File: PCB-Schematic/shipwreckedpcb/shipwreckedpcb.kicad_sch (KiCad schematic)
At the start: 180 parts, among them J1 USB4105, J14 Conn_01x01, J15 Conn_01x01, J16 Conn_01x01, J17 Conn_01x01, J18 Conn_01x01, J19 Conn_01x01, J2 Waveshare 1.54" E-Ink, J20 Conn_01x01, J21 Conn_01x01, J22 Conn_01x01, J23 Conn_01x01, J24 Conn_01x01, J25 Conn_01x01, J26 Conn_01x01, J28 Conn_01x01, J29 Conn_01x01, J3 Conn_01x01, J30 Conn_01x01, J31 Conn_01x01, J32 Conn_01x01, J33 Conn_01x01, J34 Conn_01x01, J35 Conn_01x01, J36 Conn_01x01, J37 Conn_01x01, J38 Conn_01x01, J39 Conn_01x01, J4 Conn_01x01, J5 SWD, J6 Conn_01x01, J7 Conn_01x01, Q1 Si1308EDL, SW1 BOOTSEL, SW10 Resistive, SW11 Clicky - THT, SW12 Clicky - SMD, SW13 Clicky - THT, SW14 Clicky - SMD, SW15 Clicky - THT, SW16 Clicky - SMD, SW17 Clicky - THT, SW18 Clicky - SMD, SW19 PWR Switch, SW2 RESET, SW3 Resistive, SW4 Resistive, SW5 Resistive, SW6 Resistive, SW7 Resistive, SW8 Resistive, SW9 Resistive, U1 RP2040, U2 W25Q128JVS, U3 Si4463, U4 TPS61200DRC, U5 AS179-92LF, U7 PCA9555PW, U8 ST25DV04K-IE6S3, Y1 ABM8-272-T3, Y2 X322530MOB4SI

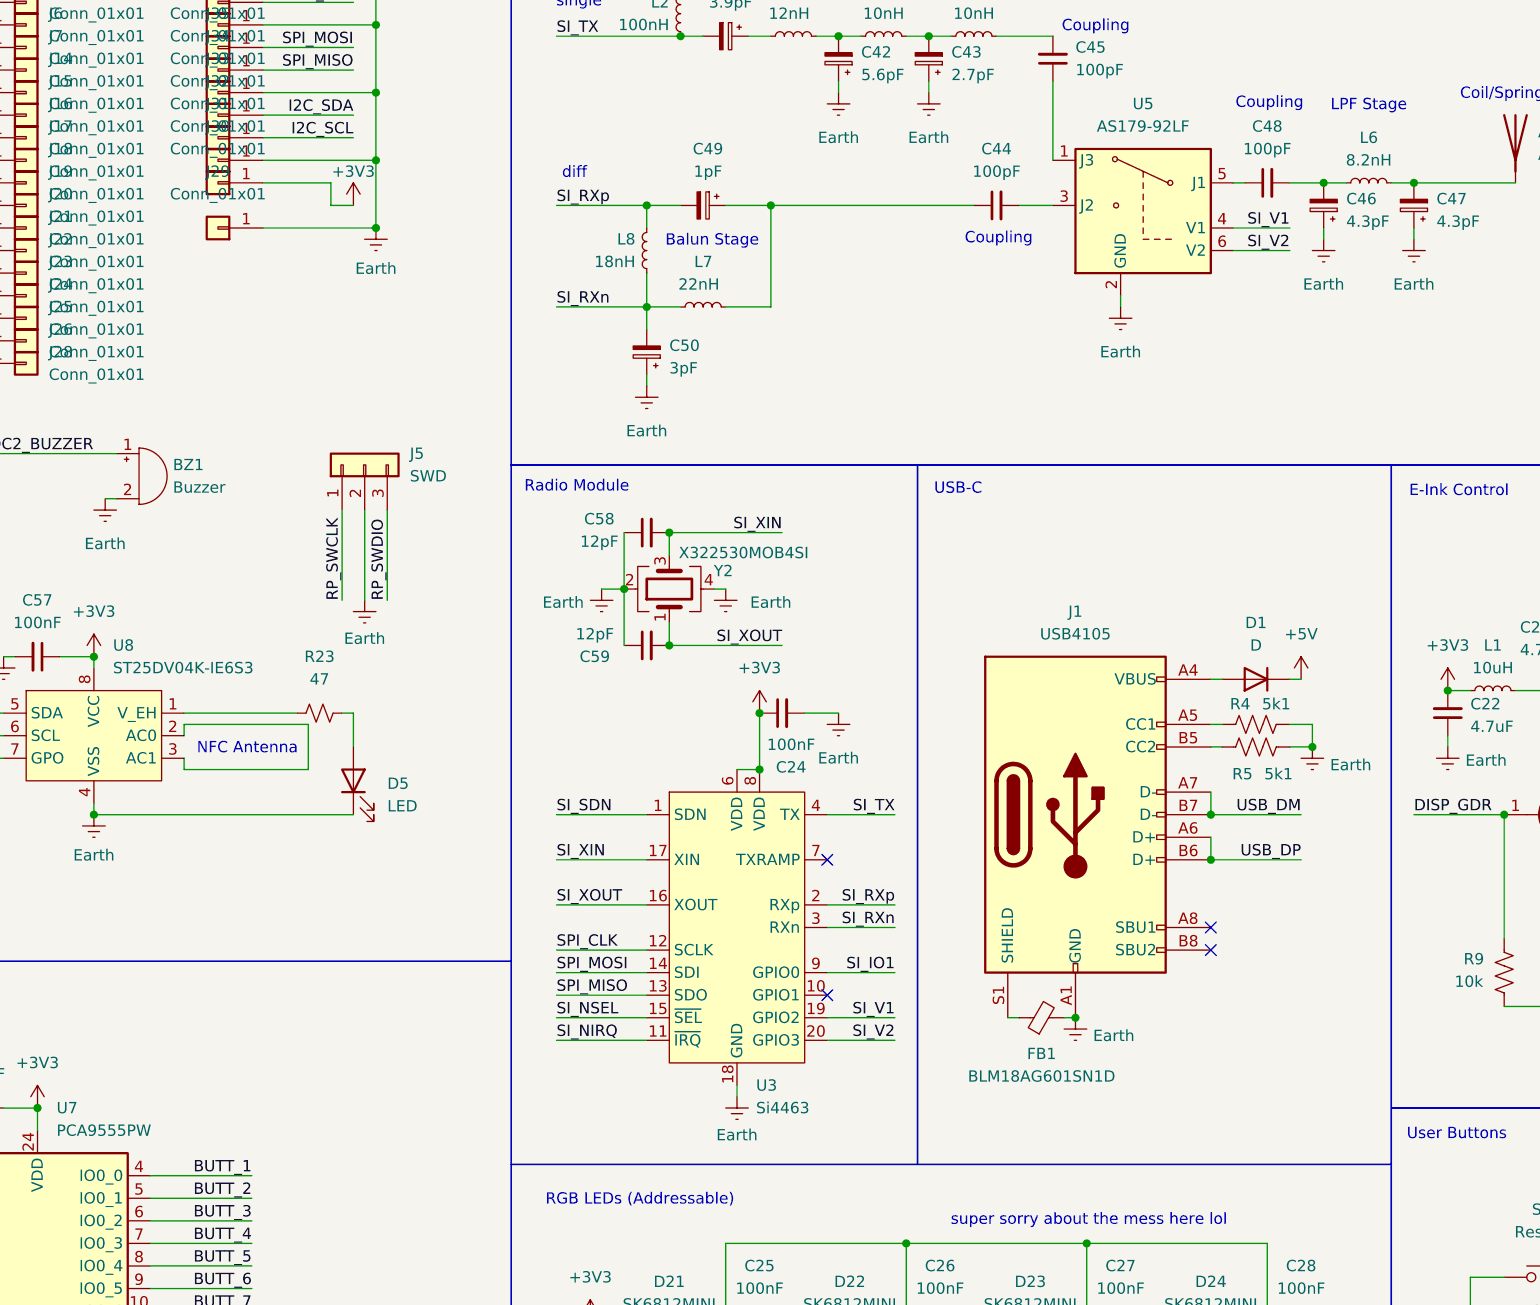
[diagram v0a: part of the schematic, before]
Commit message: boost conv, leds, caps, added ldo for usb
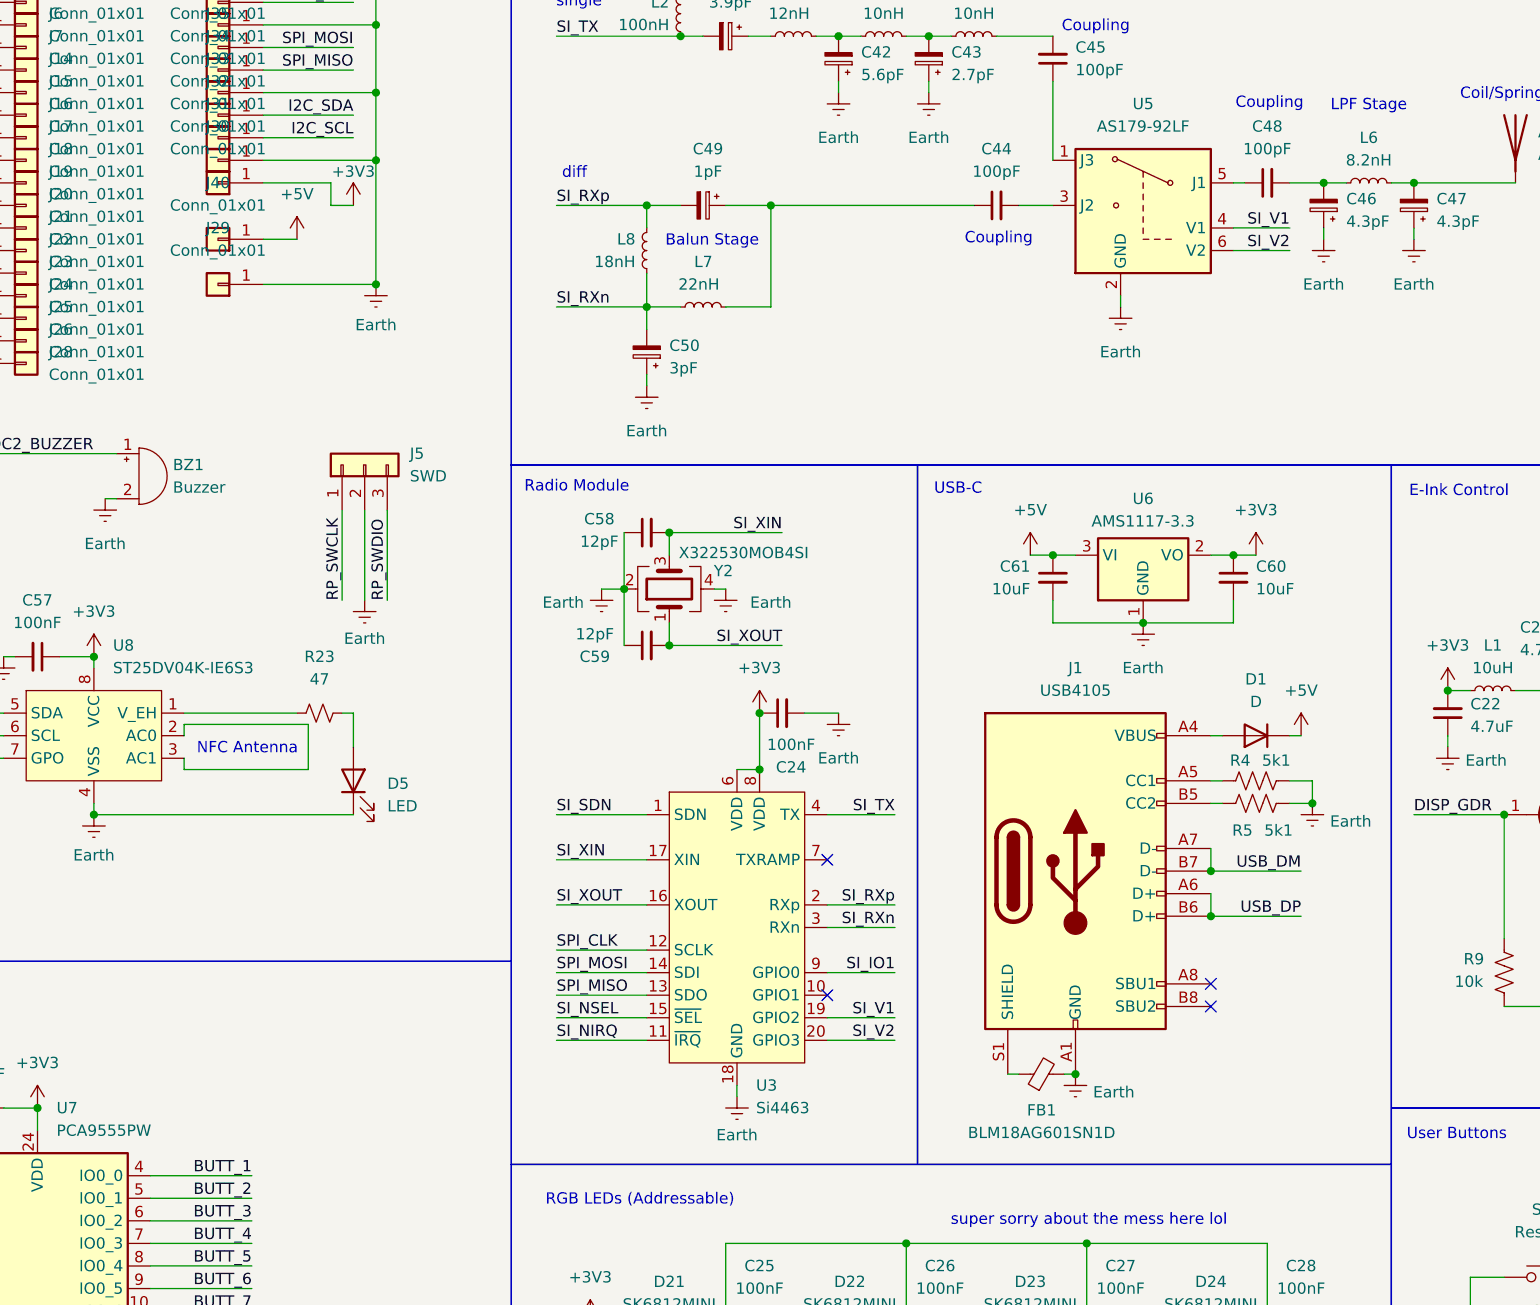
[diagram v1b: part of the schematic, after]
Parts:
- added C60, C61: 10uF, Capacitor_SMD:C_0603_1608Metric, symbol Device:C_Small
- added J40: Conn_01x01, Connector_Wire:SolderWirePad_1x01_SMD_1x2mm, symbol Connector_Generic:Conn_01x01
- added U6: AMS1117-3.3, Package_TO_SOT_SMD:SOT-223-3_TabPin2, symbol Regulator_Linear:AMS1117-3.3
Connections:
- net +3V3: now also C60.1, U6.2 (VO)
- net +5V: now also C61.1, J40.1 (Pin_1), U6.3 (VI)
- net Earth: now also C60.2, C61.2, U6.1 (GND)
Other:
- moved on the sheet: D1, FB1, J1, J29, R4, R5

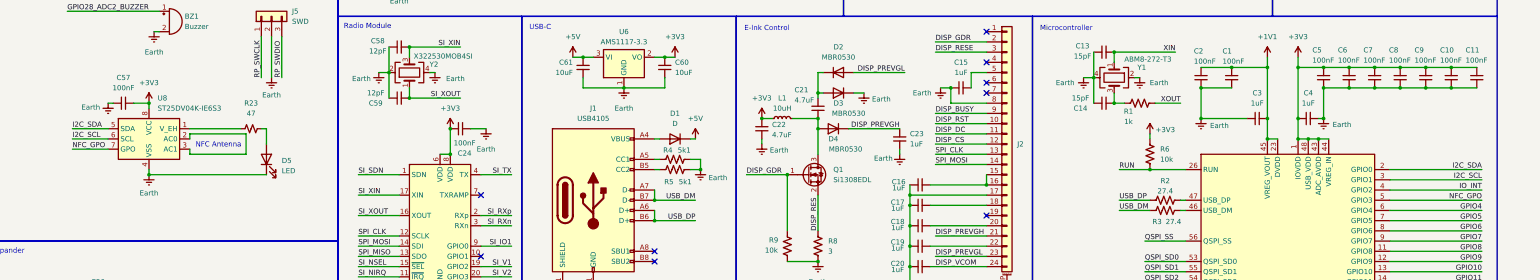
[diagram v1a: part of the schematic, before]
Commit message: finished buttons, removed nfc, routed interface headers
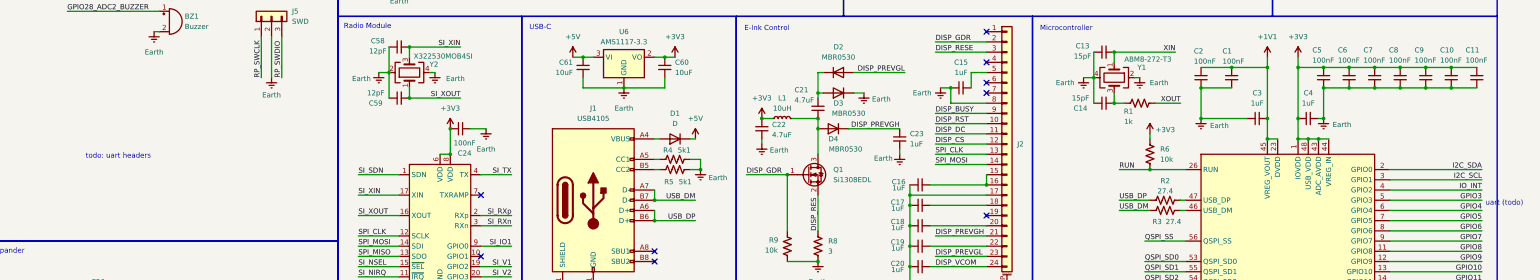
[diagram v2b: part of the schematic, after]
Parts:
- removed C57: 100nF, Capacitor_SMD:C_0603_1608Metric, symbol Device:C_Small
- removed D5: LED, LED_SMD:LED_0603_1608Metric, symbol Device:LED
- removed R23: 47, Resistor_SMD:R_0603_1608Metric, symbol Device:R_Small_US
- removed U8: ST25DV04K-IE6S3, Package_SO:SO-8_3.9x4.9mm_P1.27mm, symbol RF_NFC:ST25DV04K-IER8C3
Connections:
- net NFC_GPO renamed GPIO3
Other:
- note added: "todo: uart headers"
- note added: "uart (todo)"
- note removed: "NFC Antenna"

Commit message: finished all the gpio + buzzer
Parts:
- added J8: B2B Male, Connector_PinHeader_2.54mm:PinHeader_1x03_P2.54mm_Horizontal, symbol Connector_Generic:Conn_01x03
- added J9: B2B Female, Connector_PinSocket_2.54mm:PinSocket_1x03_P2.54mm_Horizontal, symbol Connector_Generic:Conn_01x03
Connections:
- net +3V3: now also J6.1 (Pin_1), J7.1 (Pin_1)
- net Earth: now also J8.1 (Pin_1), J9.1 (Pin_1), J9.3 (Pin_3)
- net GPIO3 renamed B2B_DCT
- net B2B_DCT: now also J8.3 (Pin_3)
- net GPIO4 renamed B2B_TX
- net B2B_TX: now also J8.2 (Pin_2); no longer J6.1 (Pin_1)
- net GPIO5 renamed B2B_RX
- net B2B_RX: now also J9.2 (Pin_2); no longer J7.1 (Pin_1)
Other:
- note removed: "todo: uart headers"
- note removed: "uart (todo)"

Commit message: started sx1262
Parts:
- added C57, C62, C63, C64, C65: tbd, Capacitor_SMD:C_0603_1608Metric, symbol Device:C_Small
- added C66: 100nF, Capacitor_SMD:C_0603_1608Metric, symbol Device:C_Small
- added C67: 470nF, Capacitor_SMD:C_0603_1608Metric, symbol Device:C_Small
- added FL1: 0900FM15K0039, RF_Converter:Balun_Johanson_0900FM15K0039, symbol Filter:0900FM15K0039
- added L10: tbd, Inductor_SMD:L_0603_1608Metric, symbol Device:L_Small
- added L11: 15uH, symbol Device:L_Small
- added R23: 100, Resistor_SMD:R_0603_1608Metric, symbol Device:R_Small_US
- added U8: SX1262IMLTRT, Package_DFN_QFN:QFN-24-1EP_4x4mm_P0.5mm_EP2.6x2.6mm, symbol RF:SX1262IMLTRT
- added U9: BGS12WN6E6327, Package_LGA:Infineon_PG-TSNP-6-10_0.7x1.1mm_0.7x1.1mm_P0.4mm, symbol RF_Switch:BGS12WN6E6327
- Y2: value X322530MOB4SI -> 32MHz
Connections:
- net +3V3: now also C65.2, C66.1, U8.1 (VDD_IN), U8.10 (VBAT), U8.11 (VBAT_IO), U9.4 (VDD)
- net Earth: now also C57.2, C62.2, C64.2, C65.1, C66.2, C67.2, FL1.10 (GND), FL1.2 (GND), FL1.5 (GND), FL1.7 (GND), FL1.9 (GND), U8.2 (GND), U8.20 (GND), U8.25 (GND), U8.5 (GND), U8.8 (GND), U9.2 (GND)
- net SI_IO1: no longer U1.28 (GPIO17)
- net SI_NIRQ: no longer U1.34 (GPIO22)
- net SI_NSEL: no longer U1.32 (GPIO21)
- net SI_SDN: no longer U1.35 (GPIO23)
- net SI_XIN: no longer C58.2, Y2.3
- net SI_XOUT: no longer C59.2, Y2.1
- net SPI_CLK: now also U8.18 (SCK)
- net SPI_MISO: now also U8.16 (MISO)
- net SPI_MOSI: now also U8.17 (MOSI)
- net at C47.2, L6.2: no longer AE1.1 (A)
- new net: FL1.6 (SW_RFI), U9.1 (RF2)
- new net: FL1.8 (SW_RFO), U9.3 (RF1)
- new net: L11.1, U8.9 (DCC_SW)
- new net: C67.1, L11.2, U8.7 (VREG)
- new net: C64.1, R23.2, U9.6 (CTRL)
- new net: AE1.1 (A), C63.2
- new net: C63.1, U9.5 (RFIN)
- new net SX_BUSY: U1.34 (GPIO22), U8.14 (BUSY)
- new net SX_DIO1: U1.28 (GPIO17), U8.13 (DIO1)
- new net SX_DIO2: R23.1, U8.12 (DIO2)
- new net SX_DIO3: U8.6 (DIO3)
- new net SX_NRST: U1.35 (GPIO23), U8.15 (~{RESET})
- new net SX_NSS: U1.32 (GPIO21), U8.19 (NSS)
- new net SX_RFI_N: FL1.3 (RFI_N), U8.22 (RFI_N)
- new net SX_RFI_P: FL1.4 (RFI_P), U8.21 (RFI_P)
- new net SX_RFO: FL1.1 (RFO), L10.2, U8.23 (RFO)
- new net SX_VR_PA: C57.1, C62.1, L10.1, U8.24 (VR_PA)
- new net SX_XTA: C58.2, U8.3 (XTA), Y2.3
- new net SX_XTB: C59.2, U8.4 (XTB), Y2.1
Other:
- note added: "unused"
- moved on the sheet: AE1, BZ1, C24, C41, C42, C43, C44, C45, C46, C47, C48, C49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

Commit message: finished prototype?
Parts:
- removed C26, C27, C28, C29, C30, C31, C32, C33, C34, C35, C36, C37, C38, C39, C40: 100nF, Capacitor_SMD:C_0603_1608Metric, symbol Device:C_Small
- removed C41: 3.9pF, Capacitor_SMD:C_0402_1005Metric, symbol Device:C_Polarized_Small
- removed C42: 5.6pF, Capacitor_SMD:C_0402_1005Metric, symbol Device:C_Polarized_Small
- removed C43: 2.7pF, Capacitor_SMD:C_0402_1005Metric, symbol Device:C_Polarized_Small
- removed C44, C45, C48: 100pF, Capacitor_SMD:C_0402_1005Metric, symbol Device:C_Small
- removed C46, C47: 4.3pF, Capacitor_SMD:C_0402_1005Metric, symbol Device:C_Polarized_Small
- removed C49: 1pF, Capacitor_SMD:C_0402_1005Metric, symbol Device:C_Polarized_Small
- removed C50: 3pF, Capacitor_SMD:C_0402_1005Metric, symbol Device:C_Polarized_Small
- removed C58, C59: 12pF, Capacitor_SMD:C_0603_1608Metric, symbol Device:C_Small
- removed D21, D22, D23, D24, D25, D26, D27, D28, D29, D30, D31, D32, D33, D34, D35, D36: SK6812MINI, LED_SMD:LED_SK6812MINI_PLCC4_3.5x3.5mm_P1.75mm, symbol LED:SK6812MINI
- removed L2: 100nH, Inductor_SMD:L_0402_1005Metric, symbol Device:L_Small
- removed L3: 12nH, Inductor_SMD:L_0402_1005Metric, symbol Device:L_Small
- removed L4, L5: 10nH, Inductor_SMD:L_0402_1005Metric, symbol Device:L_Small
- removed L6: 8.2nH, Inductor_SMD:L_0402_1005Metric, symbol Device:L_Small
- removed L7: 22nH, Inductor_SMD:L_0402_1005Metric, symbol Device:L_Small
- removed L8: 18nH, Inductor_SMD:L_0402_1005Metric, symbol Device:L_Small
- removed U3: Si4463, Package_DFN_QFN:QFN-20-1EP_4x4mm_P0.5mm_EP2.6x2.6mm_ThermalVias, symbol RF:Si4463
- removed U5: AS179-92LF, Package_TO_SOT_SMD:SOT-363_SC-70-6, symbol RF_Switch:AS179-92LF
- removed U9: BGS12WN6E6327, Package_LGA:Infineon_PG-TSNP-6-10_0.7x1.1mm_0.7x1.1mm_P0.4mm, symbol RF_Switch:BGS12WN6E6327
- added D5: LED, LED_THT:LED_D5.0mm, symbol Device:LED
- added U3: PE4259, Package_TO_SOT_SMD:SOT-363_SC-70-6, symbol RF_Switch_Extended:PE4259
- AE1, BZ1, J14, J15, J16, J17, J18, J19, J2, J20, J21, J22, J23, J24, J25, J26, J28, J29, J3, J30, J31, J32, J33, J34, J35, J36, J37, J38, J39, J4, J40, J5, J6, J7, J8, J9, JP1, JP2, JP3: now not fitted
- BT1: LCSC Part (none) -> C3029547; now not fitted
- C1, C10, C11, C12, C2, C5, C56, C6, C66, C7, C8, C9: LCSC Part (none) -> C14663
- C13, C14: LCSC Part (none) -> C107037
- C15, C16, C17, C18, C19, C20, C23, C3, C4, C52: LCSC Part (none) -> C15849
- C21, C22: LCSC Part (none) -> C1705
- C24, C25: value 100nF -> 8pF; LCSC Part (none) -> C327316
- C51, C53, C54, C55, C60, C61: LCSC Part (none) -> C19702
- C57: value tbd -> 47nF; LCSC Part (none) -> C107093
- C62: value tbd -> 47pF; LCSC Part (none) -> C105622
- C63: value tbd -> 100pF; LCSC Part (none) -> C14665
- C64: value tbd -> 1nF; LCSC Part (none) -> C100040
- C65: value tbd -> 100nF; LCSC Part (none) -> C14663
- C67: LCSC Part (none) -> C1623
- D1: footprint Diode_SMD:D_0603_1608Metric -> Diode_SMD:D_SOD-123F; LCSC Part (none) -> C2892326
- D2, D3, D4: LCSC Part (none) -> C82046
- FB1: LCSC Part (none) -> C19330
- FL1: LCSC Part (none) -> C5224443; now left out of the parts list
- J1: LCSC Part (none) -> C3020560
- L1: LCSC Part (none) -> C86083
- L10: value tbd -> 47nH; LCSC Part (none) -> C285885
- L11: footprint (none) -> Inductor_SMD:L_0805_2012Metric; LCSC Part (none) -> C383402
- L9: LCSC Part (none) -> C86423
- Q1: LCSC Part (none) -> C7603347
- R1, R7: LCSC Part (none) -> C22548
- R10, R11, R12, R13, R14, R15, R16, R17, SW10, SW3, SW4, SW5, SW6, SW7, SW8, SW9: now not fitted; now left out of the parts list
- R18: LCSC Part (none) -> C105578
- R19: LCSC Part (none) -> C2906999
- R2, R3: LCSC Part (none) -> C5126244
- R20, R21, R22, R6, R9: LCSC Part (none) -> C98220
- R23: LCSC Part (none) -> C105588
- R4, R5: LCSC Part (none) -> C2907044
- R8: LCSC Part (none) -> C2092497
- SW1, SW12, SW14, SW16, SW18, SW2: LCSC Part (none) -> C318938
- SW11, SW13, SW15, SW17: LCSC Part (none) -> C42416242
- SW19: LCSC Part (none) -> C319020
- U1: LCSC Part (none) -> C2040
- U2: LCSC Part (none) -> C97521
- U4: LCSC Part (none) -> C140320
- U6: LCSC Part (none) -> C5205141
- U7: LCSC Part (none) -> C128392
- U8: LCSC Part (none) -> C191341
- Y1: LCSC Part (none) -> C7500570
- Y2: LCSC Part (none) -> C37635386
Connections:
- net +3V3: now also U3.6 (VDD); no longer C24.1, C25.1
- net Earth: now also C24.1, C25.1, D5.1 (K), U3.2 (GND); no longer C24.2, C25.2
- net RGB_DIN: now also D5.2 (A)
- net SX_XTA: now also C24.2
- net SX_XTB: now also C25.2
- net at FL1.6 (SW_RFI): now also U3.3 (RF2)
- net at FL1.8 (SW_RFO): now also U3.1 (RF1)
- net at C64.1, R23.2: now also U3.4 (CTRL)
- net at C63.1: now also U3.5 (RFIN)
- no-connect marks 12 -> 9
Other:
- note added: "Illumination LED"
- note added: "photoresistor?"
- note removed: "Balun Stage"
- note removed: "Coupling"
- note removed: "LPF Stage"
- note removed: "Matching Stage"
- note removed: "RGB LEDs (Addressable)"
- note removed: "diff"
- note removed: "single"
- note removed: "super sorry about the mess here lol"

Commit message: fix dumb stuff
turns out you need to:
- give power :0
- add vgl cap
- not FLIP THE CONNECTOR :heavysob:
- still need to do buttons
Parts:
- added C26: 1uF, Capacitor_SMD:C_0603_1608Metric, symbol Device:C_Small
- added R24: 330, Resistor_SMD:R_0603_1608Metric, symbol Device:R_US
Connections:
- net DISP_RES is gone; now on net DISP_RESE: Q1.2 (S), R8.1
- net +3V3: now also C16.2, J2.10 (Pin_10), J2.9 (Pin_9)
- net DISP_BUSY: now also J2.16 (Pin_16); no longer J2.9 (Pin_9)
- net DISP_CS: now also J2.13 (Pin_13); no longer J2.12 (Pin_12)
- net DISP_DC: now also J2.14 (Pin_14); no longer J2.11 (Pin_11)
- net DISP_GDR: now also J2.23 (Pin_23); no longer J2.2 (Pin_2)
- net DISP_PREVGH: now also J2.4 (Pin_4); no longer J2.21 (Pin_21)
- net DISP_PREVGL: now also J2.2 (Pin_2), C26.2; no longer J2.23 (Pin_23)
- net DISP_RESE: now also J2.22 (Pin_22); no longer J2.3 (Pin_3)
- net DISP_RST: now also J2.15 (Pin_15); no longer J2.10 (Pin_10)
- net DISP_VCOM: now also J2.1 (Pin_1); no longer J2.24 (Pin_24)
- net Earth: now also C26.1
- net RGB_DIN: now also R24.1; no longer D5.2 (A)
- net SPI_CLK: now also J2.12 (Pin_12); no longer J2.13 (Pin_13)
- net SPI_MOSI: now also J2.11 (Pin_11); no longer J2.14 (Pin_14)
- net at J2.18 (Pin_18): no longer C17.2
- net at J2.20 (Pin_20): now also C15.2; no longer C18.2
- net at C19.2: now also J2.3 (Pin_3); no longer J2.22 (Pin_22)
- net at J2.5 (Pin_5): now also C18.2; no longer C15.2
- net at J2.7 (Pin_7): now also C17.2
- new net: D5.2 (A), R24.2
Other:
- note added: "Add resistive switches Select pull-up resistance"
- note removed: "Design Notes"
- note removed: "More simulation needed on radio frontend Need confirmation of display pins from River Power? how tf did I forget that Once schematic is approved, select footprints: 0603 for most parts"
- note removed: "NFC?"
- note removed: "Need to find a way to add more GPIO"
- note removed: "clicky buttons: C318938 XKB Connection TS-1101-C-W - pw switch: SK-3296S-01-L1"
- moved on the sheet: C15, C16, C17, C18, C19, C20, C21, C22, C23, C56, D2, D3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

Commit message: first pass on clicky buttons
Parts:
- removed R10, R11, R12, R13, R14, R15, R16, R17: DNF, Resistor_SMD:R_0603_1608Metric, symbol Device:R_US
- SW10, SW3, SW4, SW5, SW6, SW7, SW8, SW9: value Resistive -> Clicky - THT; footprint Resistive_Touch:Resistive_Button_130mil -> Button_Switch_THT:SW_PUSH_6mm; now fitted; now in the parts list
- SW12, SW14, SW16, SW18: value Clicky - SMD -> Clicky - THT; footprint Button_Switch_SMD:SW_Tactile_SPST_NO_Straight_CK_PTS636Sx25SMTRLFS -> Button_Switch_THT:SW_PUSH_6mm
